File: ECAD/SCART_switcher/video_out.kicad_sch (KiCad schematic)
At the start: 39 parts, among them Q29 BC857, U74 AD8054, U75 LMV331, U76 AD8054

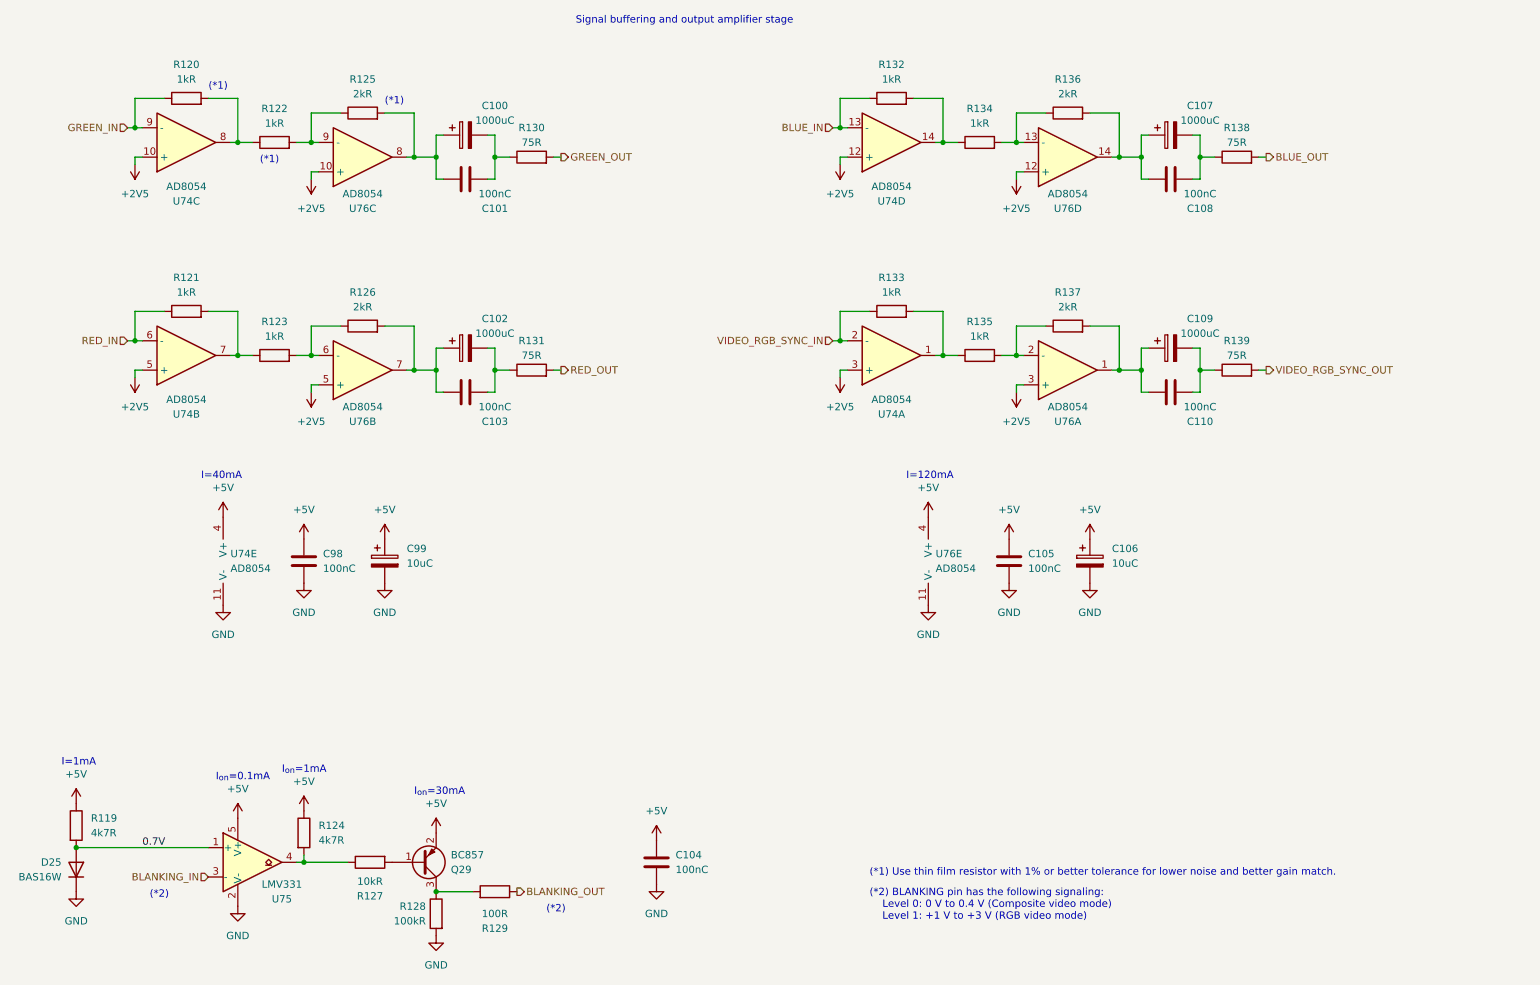
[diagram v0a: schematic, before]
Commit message: Cleanup and new power supply pcb
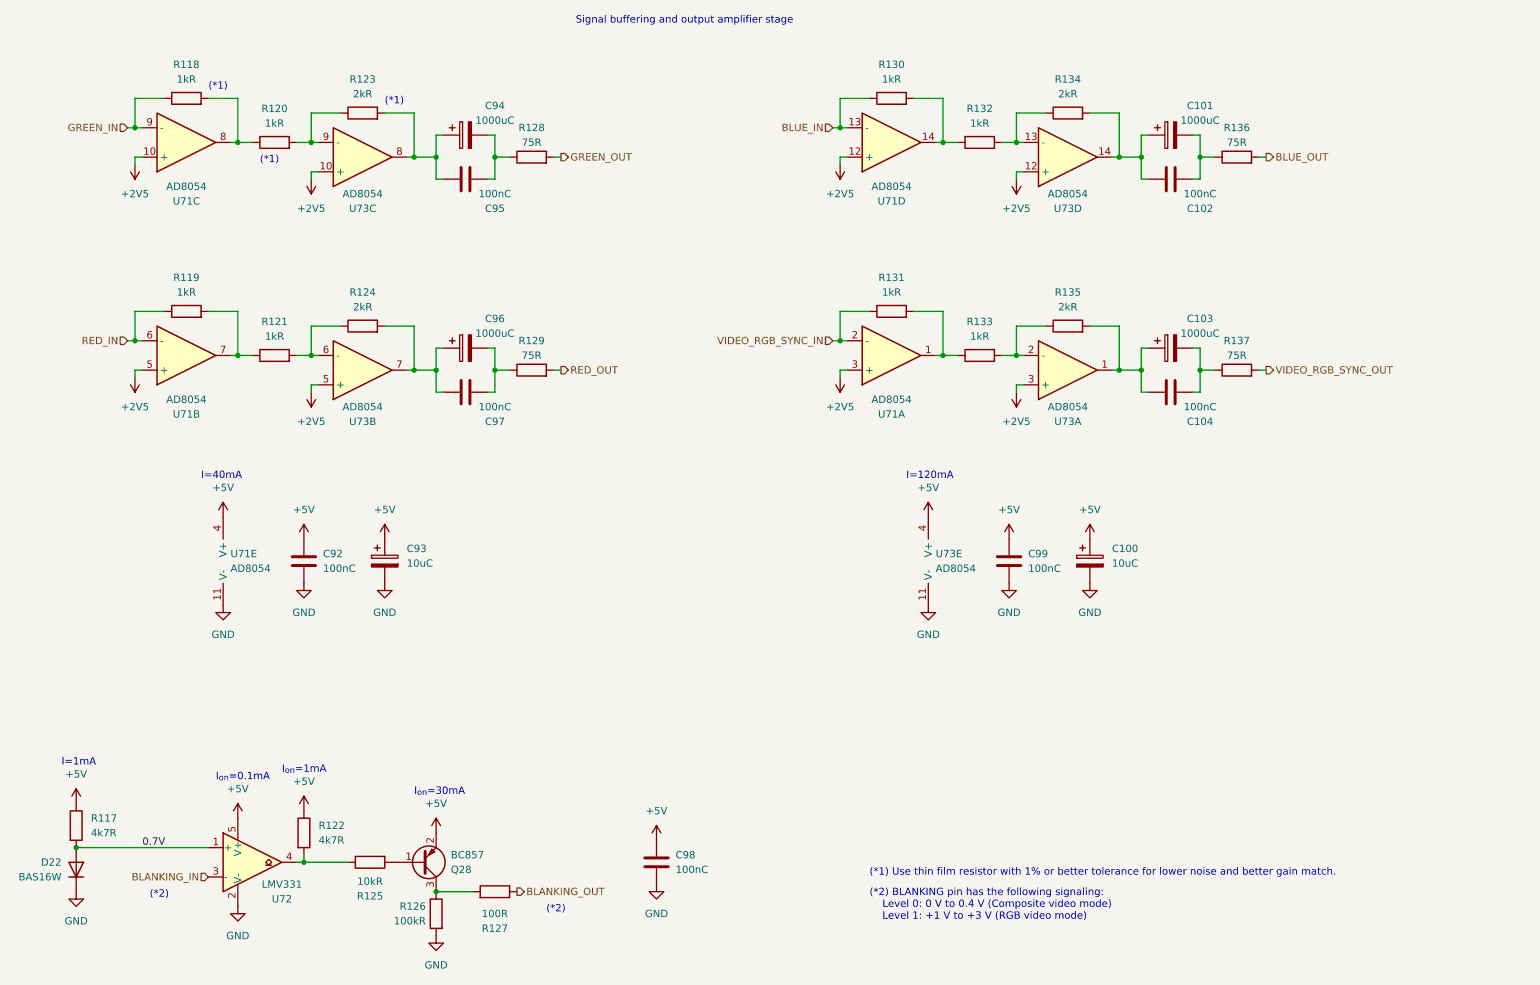
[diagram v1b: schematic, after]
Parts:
- renumbered C106 to C100, C107 to C101, C108 to C102, C109 to C103, C110 to C104, C98 to C92, C99 to C93, C100 to C94, C101 to C95, C102 to C96, C103 to C97, C104 to C98, C105 to C99, D25 to D22, Q29 to Q28, R119 to R117, R120 to R118, R121 to R119, R122 to R120, R123 to R121, R124 to R122, R125 to R123, R126 to R124, R127 to R125, R128 to R126, R129 to R127, R130 to R128, R131 to R129, R132 to R130, R133 to R131, R134 to R132, R135 to R133, R136 to R134, R137 to R135, R138 to R136, R139 to R137, U74 to U71, U75 to U72, U76 to U73

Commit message: Progressed ECAD.
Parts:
- renumbered C102 to C100, C103 to C101, C104 to C102, C92 to C90, C93 to C91, C94 to C92, C95 to C93, C96 to C94, C97 to C95, C98 to C96, C99 to C97, C100 to C98, C101 to C99

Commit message: Progressed ECAD.
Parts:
- renumbered R117 to R119, R118 to R120, R119 to R121, R120 to R122, R121 to R123, R122 to R124, R123 to R125, R124 to R126, R125 to R127, R126 to R128, R127 to R129, R128 to R130, R129 to R131, R130 to R132, R131 to R133, R132 to R134, R133 to R135, R134 to R136, R135 to R137, R136 to R138, R137 to R139

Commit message: Progressed ECAD.
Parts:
- R127: MPN RC0805FR-0710KL -> AC0805FR-0710KL; Status (none) -> OK
- R128: MPN (none) -> RC0805FR-07100KL; Status (none) -> OK
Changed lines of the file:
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@@
       (effects (font (size 1.27 1.27)) hide)
     )
-    (property "Datasheet" "https://datasheet.lcsc.com/lcsc/1810201611_YAGEO-RC0805FR-0710KL_C84376.pdf" (at 91.44 166.37 0)
-      (effects (font (size 1.27 1.27)) hide)
-    )
-    (property "MPN" "RC0805FR-0710KL" (at 91.44 166.37 0)
-      (effects (font (size 1.27 1.27)) hide)
-    )
-    (property "Status" "" (at 91.44 166.37 0)
+    (property "Datasheet" "https://datasheet.lcsc.com/lcsc/2304140030_YAGEO-AC0805FR-0710KL_C140868.pdf" (at 91.44 166.37 0)
+      (effects (font (size 1.27 1.27)) hide)
+    )
+    (property "MPN" "AC0805FR-0710KL" (at 91.44 166.37 0)
+      (effects (font (size 1.27 1.27)) hide)
+    )
+    (property "Status" "OK" (at 91.44 166.37 0)
       (effects (font (size 1.27 1.27)) hide)
     )
@@
       (effects (font (size 1.27 1.27)) hide)
     )
-    (property "Datasheet" "~" (at 102.87 175.26 0)
-      (effects (font (size 1.27 1.27)) hide)
-    )
-    (property "Status" "" (at 102.87 175.26 0)
-      (effects (font (size 1.27 1.27)) hide)
-    )
+    (property "Datasheet" "https://datasheet.lcsc.com/lcsc/2304140030_YAGEO-RC0805FR-07100KL_C96346.pdf" (at 102.87 175.26 0)
+      (effects (font (size 1.27 1.27)) hide)
+    )
+    (property "Status" "OK" (at 102.87 175.26 0)
+      (effects (font (size 1.27 1.27)) hide)
+    )
+    (property "MPN" "RC0805FR-07100KL" (at 102.87 175.26 0)
+      (effects (font (size 1.27 1.27)) hide)
+    )

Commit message: Progressed ECAD.
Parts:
- C90, C96, C97: MPN CL21B104KBCNNNC -> CL10B104KO8NNNC; Status (none) -> OK
- R119, R124: MPN (none) -> RT0805FRE074K7L; Status (none) -> OK
- R120, R121, R122, R123, R132, R133, R134, R135: MPN (none) -> RT0805BRD071KL; Status (none) -> OK
- R125, R126, R136, R137: MPN (none) -> RT0805BRE072KL; Status (none) -> OK
- R129: MPN (none) -> RT0805BRD07100RL; Status (none) -> OK
- R130, R131, R138, R139: MPN (none) -> AC1210FR-0775RL; Status (none) -> OK

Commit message: Progressed ECAD.
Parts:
- D72: renamed from D22; MPN_MOUSER (none) -> BAS16W,115
- Q28: MPN_MOUSER (none) -> BC857C,215
- U71, U73: footprint Package_SO:TSSOP-14_4.4x5mm_P0.65mm -> Package_SO:SOIC-14_3.9x8.7mm_P1.27mm; MPN GS8054-TR -> OPA4354AIDR; MPN_MOUSER (none) -> AD8054ARZ-REEL7; Status (none) -> OK
- U72: MPN_MOUSER (none) -> LMV331IDBVR

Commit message: Progressed ECAD.
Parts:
- removed D72: BAS16W, Package_TO_SOT_SMD:SOT-323_SC-70, symbol Diode:BAS16W
- added D72: BAS16H, Diode_SMD:D_SOD-123F, symbol Diode:BAS316
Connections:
- net 0.7V: now also D72.2 (A)
- net GND: now also D72.1 (K)
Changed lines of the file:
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@@
   (junction (at 99.06 81.28) (diameter 0) (color 0 0 0 0)
   )
+  (junction (at 50.8 39.37) (diameter 0) (color 0 0 0 0)
+  )
+  (junction (at 113.03 44.45) (diameter 0) (color 0 0 0 0)
+  )
+  (junction (at 81.28 41.91) (diameter 0) (color 0 0 0 0)
+  )
+  (junction (at 102.87 81.28) (diameter 0) (color 0 0 0 0)
+  )
+  (junction (at 203.2 41.91) (diameter 0) (color 0 0 0 0)
+  )
+  (junction (at 102.87 44.45) (diameter 0) (color 0 0 0 0)
+  )
+  (junction (at 234.95 44.45) (diameter 0) (color 0 0 0 0)
+  )
+  (junction (at 99.06 44.45) (diameter 0) (color 0 0 0 0)
+  )
+  (junction (at 172.72 76.2) (diameter 0) (color 0 0 0 0)
+  )
+  (junction (at 113.03 81.28) (diameter 0) (color 0 0 0 0)
+  )
+  (junction (at 68.58 78.74) (diameter 0) (color 0 0 0 0)
+  )
+  (junction (at 203.2 78.74) (diameter 0) (color 0 0 0 0)
+  )
+  (junction (at 224.79 81.28) (diameter 0) (color 0 0 0 0)
+  )
+  (junction (at 102.87 171.45) (diameter 0) (color 0 0 0 0)
+  )
+  (junction (at 172.72 39.37) (diameter 0) (color 0 0 0 0)
+  )
+  (junction (at 190.5 78.74) (diameter 0) (color 0 0 0 0)
+  )
   (junction (at 40.64 163.83) (diameter 0) (color 0 0 0 0)
-  )
-  (junction (at 50.8 39.37) (diameter 0) (color 0 0 0 0)
-  )
-  (junction (at 113.03 44.45) (diameter 0) (color 0 0 0 0)
-  )
-  (junction (at 81.28 41.91) (diameter 0) (color 0 0 0 0)
-  )
-  (junction (at 102.87 81.28) (diameter 0) (color 0 0 0 0)
-  )
-  (junction (at 203.2 41.91) (diameter 0) (color 0 0 0 0)
-  )
-  (junction (at 102.87 44.45) (diameter 0) (color 0 0 0 0)
-  )
-  (junction (at 234.95 44.45) (diameter 0) (color 0 0 0 0)
-  )
-  (junction (at 99.06 44.45) (diameter 0) (color 0 0 0 0)
-  )
-  (junction (at 172.72 76.2) (diameter 0) (color 0 0 0 0)
-  )
-  (junction (at 113.03 81.28) (diameter 0) (color 0 0 0 0)
-  )
-  (junction (at 68.58 78.74) (diameter 0) (color 0 0 0 0)
-  )
-  (junction (at 203.2 78.74) (diameter 0) (color 0 0 0 0)
-  )
-  (junction (at 224.79 81.28) (diameter 0) (color 0 0 0 0)
-  )
-  (junction (at 102.87 171.45) (diameter 0) (color 0 0 0 0)
-  )
-  (junction (at 172.72 39.37) (diameter 0) (color 0 0 0 0)
-  )
-  (junction (at 190.5 78.74) (diameter 0) (color 0 0 0 0)
   )
   (junction (at 224.79 44.45) (diameter 0) (color 0 0 0 0)
@@
         (path "/8cd08eb5-4755-4ef5-8eeb-77fd9974b180/6562ea38-5963-42b2-a0ef-a4a12a4c652f/ad3a0592-e2c6-4827-8dd3-54afc0bdac28"
           (reference "C93") (unit 1)
+        )
+      )
+    )
+  )
+  (symbol (lib_id "Diode:BAS316") (at 40.64 167.64 270) (mirror x) (unit 1)
+    (in_bom yes) (on_board yes) (dnp no)
+    (property "Reference" "D72" (at 38.1 166.37 90)
+      (effects (font (size 1.27 1.27)) (justify right))
+    )
+    (property "Value" "BAS16H" (at 38.1 168.91 90)
+      (effects (font (size 1.27 1.27)) (justify right))
+    )
+    (property "Footprint" "Diode_SMD:D_SOD-123F" (at 36.195 167.64 0)
+      (effects (font (size 1.27 1.27)) hide)
+    )
+    (property "Datasheet" "https://datasheet.lcsc.com/lcsc/2304140030_Nexperia-BAS16H-115_C130413.pdf" (at 40.64 167.64 0)
+      (effects (font (size 1.27 1.27)) hide)
+    )
+    (property "MPN" "BAS16H,115" (at 40.64 167.64 0)
+      (effects (font (size 1.27 1.27)) hide)
+    )
+    (property "MPN_MOUSER" "BAS16H,115" (at 40.64 167.64 0)
+      (effects (font (size 1.27 1.27)) hide)
+    )
+    (property "Status" "OK" (at 40.64 167.64 0)
+      (effects (font (size 1.27 1.27)) hide)
+    )
+    (pin "2")
+    (pin "1")
+    (instances
+      (project "SCART_switcher"
+        (path "/8cd08eb5-4755-4ef5-8eeb-77fd9974b180/6562ea38-5963-42b2-a0ef-a4a12a4c652f/ad3a0592-e2c6-4827-8dd3-54afc0bdac28"
+          (reference "D72") (unit 1)
         )
       )
@@
         )
       )
-    )
-  )
-  (symbol (lib_id "Diode:BAS16W") (at 40.64 167.64 270) (mirror x) (unit 1)
-    (in_bom yes) (on_board yes) (dnp no)
-    (property "Reference" "D72" (at 38.1 166.37 90)
-      (effects (font (size 1.27 1.27)) (justify right))
-    )
-    (property "Value" "BAS16W" (at 38.1 168.91 90)
-      (effects (font (size 1.27 1.27)) (justify right))
-    )
-    (property "Footprint" "Package_TO_SOT_SMD:SOT-323_SC-70" (at 36.195 167.64 0)
-      (effects (font (size 1.27 1.27)) hide)
-    )
-    (property "Datasheet" "https://datasheet.lcsc.com/lcsc/2304140030_Nexperia-BAS16W-115_C56624.pdf" (at 40.64 167.64 0)
-      (effects (font (size 1.27 1.27)) hide)
-    )
-    (property "Status" "OK" (at 40.64 167.64 0)
-      (effects (font (size 1.27 1.27)) hide)
-    )
-    (property "MPN" "BAS16W,115" (at 40.64 167.64 0)
-      (effects (font (size 1.27 1.27)) hide)
-    )
-    (property "MPN_MOUSER" "BAS16W,115" (at 40.64 167.64 0)
-      (effects (font (size 1.27 1.27)) hide)
-    )
-    (pin "1")
-    (pin "2")
-    (pin "3")
-    (instances
-      (project "SCART_switcher"
-        (path "/8cd08eb5-4755-4ef5-8eeb-77fd9974b180/6562ea38-5963-42b2-a0ef-a4a12a4c652f/ad3a0592-e2c6-4827-8dd3-54afc0bdac28"
-          (reference "D72") (unit 1)
-        )
-      )

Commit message: Progressed ECAD.
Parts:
- U71, U73: value AD8054 -> OPA4354; MPN_MOUSER AD8054ARZ-REEL7 -> OPA4354AIDR
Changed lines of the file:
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@@
       (effects (font (size 1.27 1.27)) (justify left))
     )
-    (property "Value" "AD8054" (at 189.23 115.57 0)
+    (property "Value" "OPA4354" (at 189.23 115.57 0)
       (effects (font (size 1.27 1.27)) (justify left))
     )
@@
       (effects (font (size 1.27 1.27)) hide)
     )
-    (property "Datasheet" "https://datasheet.lcsc.com/lcsc/2310091129_Analog-Devices-AD8054ARU-REEL_C4368882.pdf" (at 190.5 114.3 0)
+    (property "Datasheet" "https://datasheet.lcsc.com/lcsc/1912111437_Texas-Instruments-OPA4354AIDR_C440031.pdf" (at 190.5 114.3 0)
       (effects (font (size 1.27 1.27)) hide)
     )
@@
       (effects (font (size 1.27 1.27)) hide)
     )
-    (property "MPN_MOUSER" "AD8054ARZ-REEL7" (at 190.5 114.3 0)
+    (property "MPN_MOUSER" "OPA4354AIDR" (at 190.5 114.3 0)
       (effects (font (size 1.27 1.27)) hide)
     )
@@
       (effects (font (size 1.27 1.27)))
     )
-    (property "Value" "AD8054" (at 212.09 50.8 0)
+    (property "Value" "OPA4354" (at 212.09 50.8 0)
       (effects (font (size 1.27 1.27)))
     )
@@
       (effects (font (size 1.27 1.27)) hide)
     )
-    (property "Datasheet" "https://datasheet.lcsc.com/lcsc/2310091129_Analog-Devices-AD8054ARU-REEL_C4368882.pdf" (at 212.09 44.45 0)
+    (property "Datasheet" "https://datasheet.lcsc.com/lcsc/1912111437_Texas-Instruments-OPA4354AIDR_C440031.pdf" (at 212.09 44.45 0)
       (effects (font (size 1.27 1.27)) hide)
     )
@@
       (effects (font (size 1.27 1.27)) hide)
     )
-    (property "MPN_MOUSER" "AD8054ARZ-REEL7" (at 212.09 44.45 0)
+    (property "MPN_MOUSER" "OPA4354AIDR" (at 212.09 44.45 0)
       (effects (font (size 1.27 1.27)) hide)
     )
@@
       (effects (font (size 1.27 1.27)))
     )
-    (property "Value" "AD8054" (at 90.17 87.63 0)
+    (property "Value" "OPA4354" (at 90.17 87.63 0)
       (effects (font (size 1.27 1.27)))
     )
@@
       (effects (font (size 1.27 1.27)) hide)
     )
-    (property "Datasheet" "https://datasheet.lcsc.com/lcsc/2310091129_Analog-Devices-AD8054ARU-REEL_C4368882.pdf" (at 90.17 81.28 0)
+    (property "Datasheet" "https://datasheet.lcsc.com/lcsc/1912111437_Texas-Instruments-OPA4354AIDR_C440031.pdf" (at 90.17 81.28 0)
       (effects (font (size 1.27 1.27)) hide)
     )
@@
       (effects (font (size 1.27 1.27)) hide)
     )
-    (property "MPN_MOUSER" "AD8054ARZ-REEL7" (at 90.17 81.28 0)
+    (property "MPN_MOUSER" "OPA4354AIDR" (at 90.17 81.28 0)
       (effects (font (size 1.27 1.27)) hide)
     )
@@
       (effects (font (size 1.27 1.27)))
     )
-    (property "Value" "AD8054" (at 181.61 49.53 0)
+    (property "Value" "OPA4354" (at 181.61 49.53 0)
       (effects (font (size 1.27 1.27)))
     )
@@
       (effects (font (size 1.27 1.27)) hide)
     )
-    (property "Datasheet" "https://datasheet.lcsc.com/lcsc/2310091129_Analog-Devices-AD8054ARU-REEL_C4368882.pdf" (at 181.61 41.91 0)
+    (property "Datasheet" "https://datasheet.lcsc.com/lcsc/1912111437_Texas-Instruments-OPA4354AIDR_C440031.pdf" (at 181.61 41.91 0)
       (effects (font (size 1.27 1.27)) hide)
     )
@@
       (effects (font (size 1.27 1.27)) hide)
     )
-    (property "MPN_MOUSER" "AD8054ARZ-REEL7" (at 181.61 41.91 0)
+    (property "MPN_MOUSER" "OPA4354AIDR" (at 181.61 41.91 0)
       (effects (font (size 1.27 1.27)) hide)
     )
@@
       (effects (font (size 1.27 1.27)))
     )
-    (property "Value" "AD8054" (at 59.69 86.36 0)
+    (property "Value" "OPA4354" (at 59.69 86.36 0)
       (effects (font (size 1.27 1.27)))
     )
@@
       (effects (font (size 1.27 1.27)) hide)
     )
-    (property "Datasheet" "https://datasheet.lcsc.com/lcsc/2310091129_Analog-Devices-AD8054ARU-REEL_C4368882.pdf" (at 59.69 78.74 0)
+    (property "Datasheet" "https://datasheet.lcsc.com/lcsc/1912111437_Texas-Instruments-OPA4354AIDR_C440031.pdf" (at 59.69 78.74 0)
       (effects (font (size 1.27 1.27)) hide)
     )
@@
       (effects (font (size 1.27 1.27)) hide)
     )
-    (property "MPN_MOUSER" "AD8054ARZ-REEL7" (at 59.69 78.74 0)
+    (property "MPN_MOUSER" "OPA4354AIDR" (at 59.69 78.74 0)
       (effects (font (size 1.27 1.27)) hide)
     )
@@
       (effects (font (size 1.27 1.27)) (justify left))
     )
-    (property "Value" "AD8054" (at 67.31 115.57 0)
+    (property "Value" "OPA4354" (at 67.31 115.57 0)
       (effects (font (size 1.27 1.27)) (justify left))
     )
@@
       (effects (font (size 1.27 1.27)) hide)
     )
-    (property "Datasheet" "https://datasheet.lcsc.com/lcsc/2310091129_Analog-Devices-AD8054ARU-REEL_C4368882.pdf" (at 68.58 114.3 0)
+    (property "Datasheet" "https://datasheet.lcsc.com/lcsc/1912111437_Texas-Instruments-OPA4354AIDR_C440031.pdf" (at 68.58 114.3 0)
       (effects (font (size 1.27 1.27)) hide)
     )
@@
       (effects (font (size 1.27 1.27)) hide)
     )
-    (property "MPN_MOUSER" "AD8054ARZ-REEL7" (at 68.58 114.3 0)
+    (property "MPN_MOUSER" "OPA4354AIDR" (at 68.58 114.3 0)
       (effects (font (size 1.27 1.27)) hide)
     )
@@
       (effects (font (size 1.27 1.27)))
     )
-    (property "Value" "AD8054" (at 181.61 86.36 0)
+    (property "Value" "OPA4354" (at 181.61 86.36 0)
       (effects (font (size 1.27 1.27)))
     )
@@
       (effects (font (size 1.27 1.27)) hide)
     )
-    (property "Datasheet" "https://datasheet.lcsc.com/lcsc/2310091129_Analog-Devices-AD8054ARU-REEL_C4368882.pdf" (at 181.61 78.74 0)
+    (property "Datasheet" "https://datasheet.lcsc.com/lcsc/1912111437_Texas-Instruments-OPA4354AIDR_C440031.pdf" (at 181.61 78.74 0)
       (effects (font (size 1.27 1.27)) hide)
     )
@@
       (effects (font (size 1.27 1.27)) hide)
     )
-    (property "MPN_MOUSER" "AD8054ARZ-REEL7" (at 181.61 78.74 0)
+    (property "MPN_MOUSER" "OPA4354AIDR" (at 181.61 78.74 0)
       (effects (font (size 1.27 1.27)) hide)
     )
@@
       (effects (font (size 1.27 1.27)))
     )
-    (property "Value" "AD8054" (at 59.69 49.53 0)
+    (property "Value" "OPA4354" (at 59.69 49.53 0)
       (effects (font (size 1.27 1.27)))
     )
@@
       (effects (font (size 1.27 1.27)) hide)
     )
-    (property "Datasheet" "https://datasheet.lcsc.com/lcsc/2310091129_Analog-Devices-AD8054ARU-REEL_C4368882.pdf" (at 59.69 41.91 0)
+    (property "Datasheet" "https://datasheet.lcsc.com/lcsc/1912111437_Texas-Instruments-OPA4354AIDR_C440031.pdf" (at 59.69 41.91 0)
       (effects (font (size 1.27 1.27)) hide)
     )
@@
       (effects (font (size 1.27 1.27)) hide)
     )
-    (property "MPN_MOUSER" "AD8054ARZ-REEL7" (at 59.69 41.91 0)
+    (property "MPN_MOUSER" "OPA4354AIDR" (at 59.69 41.91 0)
       (effects (font (size 1.27 1.27)) hide)
     )
@@
       (effects (font (size 1.27 1.27)))
     )
-    (property "Value" "AD8054" (at 212.09 87.63 0)
+    (property "Value" "OPA4354" (at 212.09 87.63 0)
       (effects (font (size 1.27 1.27)))
     )
@@
       (effects (font (size 1.27 1.27)) hide)
     )
-    (property "Datasheet" "https://datasheet.lcsc.com/lcsc/2310091129_Analog-Devices-AD8054ARU-REEL_C4368882.pdf" (at 212.09 81.28 0)
+    (property "Datasheet" "https://datasheet.lcsc.com/lcsc/1912111437_Texas-Instruments-OPA4354AIDR_C440031.pdf" (at 212.09 81.28 0)
       (effects (font (size 1.27 1.27)) hide)
     )
@@
       (effects (font (size 1.27 1.27)) hide)
     )
-    (property "MPN_MOUSER" "AD8054ARZ-REEL7" (at 212.09 81.28 0)
+    (property "MPN_MOUSER" "OPA4354AIDR" (at 212.09 81.28 0)
       (effects (font (size 1.27 1.27)) hide)
     )
@@
       (effects (font (size 1.27 1.27)))
     )
-    (property "Value" "AD8054" (at 90.17 50.8 0)
+    (property "Value" "OPA4354" (at 90.17 50.8 0)
       (effects (font (size 1.27 1.27)))
     )
@@
       (effects (font (size 1.27 1.27)) hide)
     )
-    (property "Datasheet" "https://datasheet.lcsc.com/lcsc/2310091129_Analog-Devices-AD8054ARU-REEL_C4368882.pdf" (at 90.17 44.45 0)
+    (property "Datasheet" "https://datasheet.lcsc.com/lcsc/1912111437_Texas-Instruments-OPA4354AIDR_C440031.pdf" (at 90.17 44.45 0)
       (effects (font (size 1.27 1.27)) hide)
     )
@@
       (effects (font (size 1.27 1.27)) hide)
     )
-    (property "MPN_MOUSER" "AD8054ARZ-REEL7" (at 90.17 44.45 0)
-      (effects (font (size 1.27 1.27)) hide)
-    )
+    (property "MPN_MOUSER" "OPA4354AIDR" (at 90.17 44.45 0)
+      (effects (font (size 1.27 1.27)) hide)
+    )
